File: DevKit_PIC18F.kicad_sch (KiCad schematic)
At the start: 29 parts, among them J1 PIC_ICSP_ICD, J2 USB_B, J3 5P_UART, J4 RA_PORT, J5 RB_PORT, J6 RD_PORT, J7 RC_PORT, J8 RE_PORT, SW1 SW_DIP, X1 16MHz

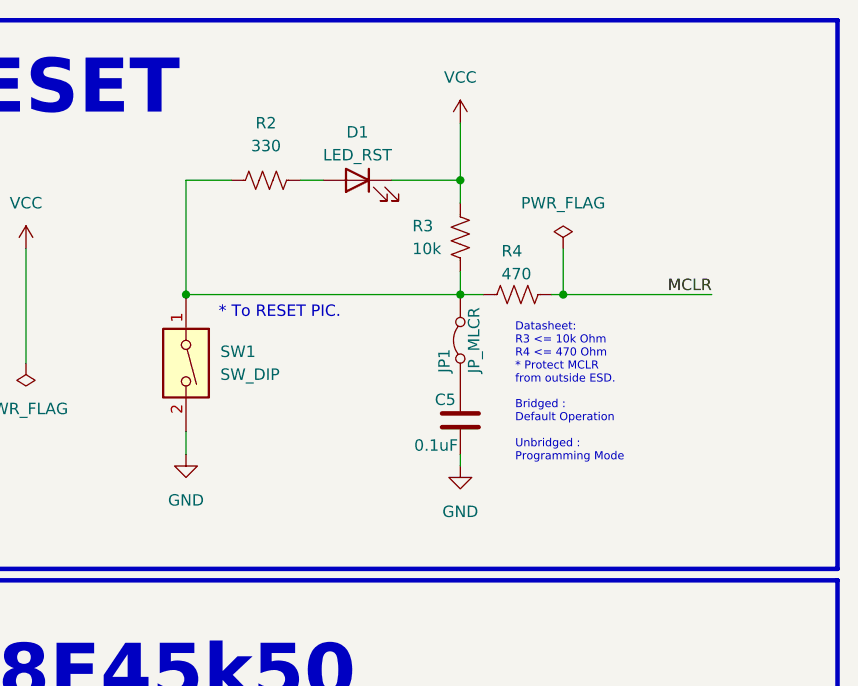
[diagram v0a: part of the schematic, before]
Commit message: Fix Bug : remove bridge as we don't need it.
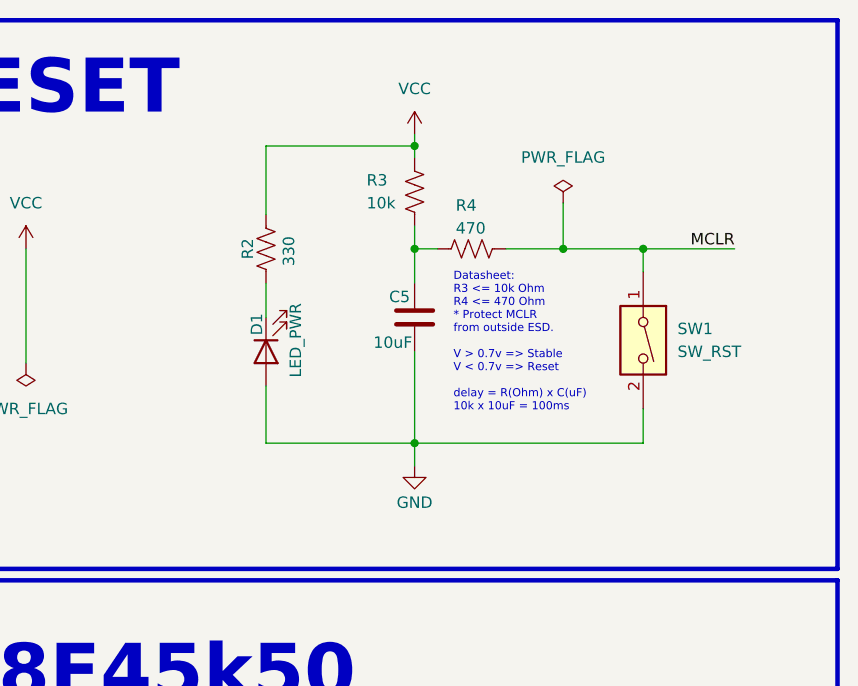
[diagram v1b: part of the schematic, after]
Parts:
- removed JP1: JP_MLCR, Button_Switch_THT:SW_DIP_SPSTx01_Slide_9.78x4.72mm_W7.62mm_P2.54mm, symbol Jumper:Jumper_2_Bridged
- C5: value 0.1uF -> 10uF
- D1: value LED_RST -> LED_PWR
- SW1: value SW_DIP -> SW_RST
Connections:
- net GND: now also D1.2 (A)
- net MCLR: now also SW1.1
- net VCC: now also R2.2; no longer D1.1 (K)
- net at R3.2, R4.2: now also C5.2; no longer R2.1, SW1.1
- new net: D1.1 (K), R2.1
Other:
- note added: "Datasheet: R3 <= 10k Ohm R4 <= 470 Ohm * Protect MCLR from outside ESD. V > 0.7v => Stable V < 0.7v => Reset delay = R(Ohm) x C(uF) 10k x 10uF = 100ms"
- note removed: "* To RESET PIC."
- note removed: "Bridged : Default Operation Unbridged : Programming Mode"
- note removed: "Datasheet: R3 <= 10k Ohm R4 <= 470 Ohm * Protect MCLR from outside ESD."
- moved on the sheet: C5, R3, R4, SW1

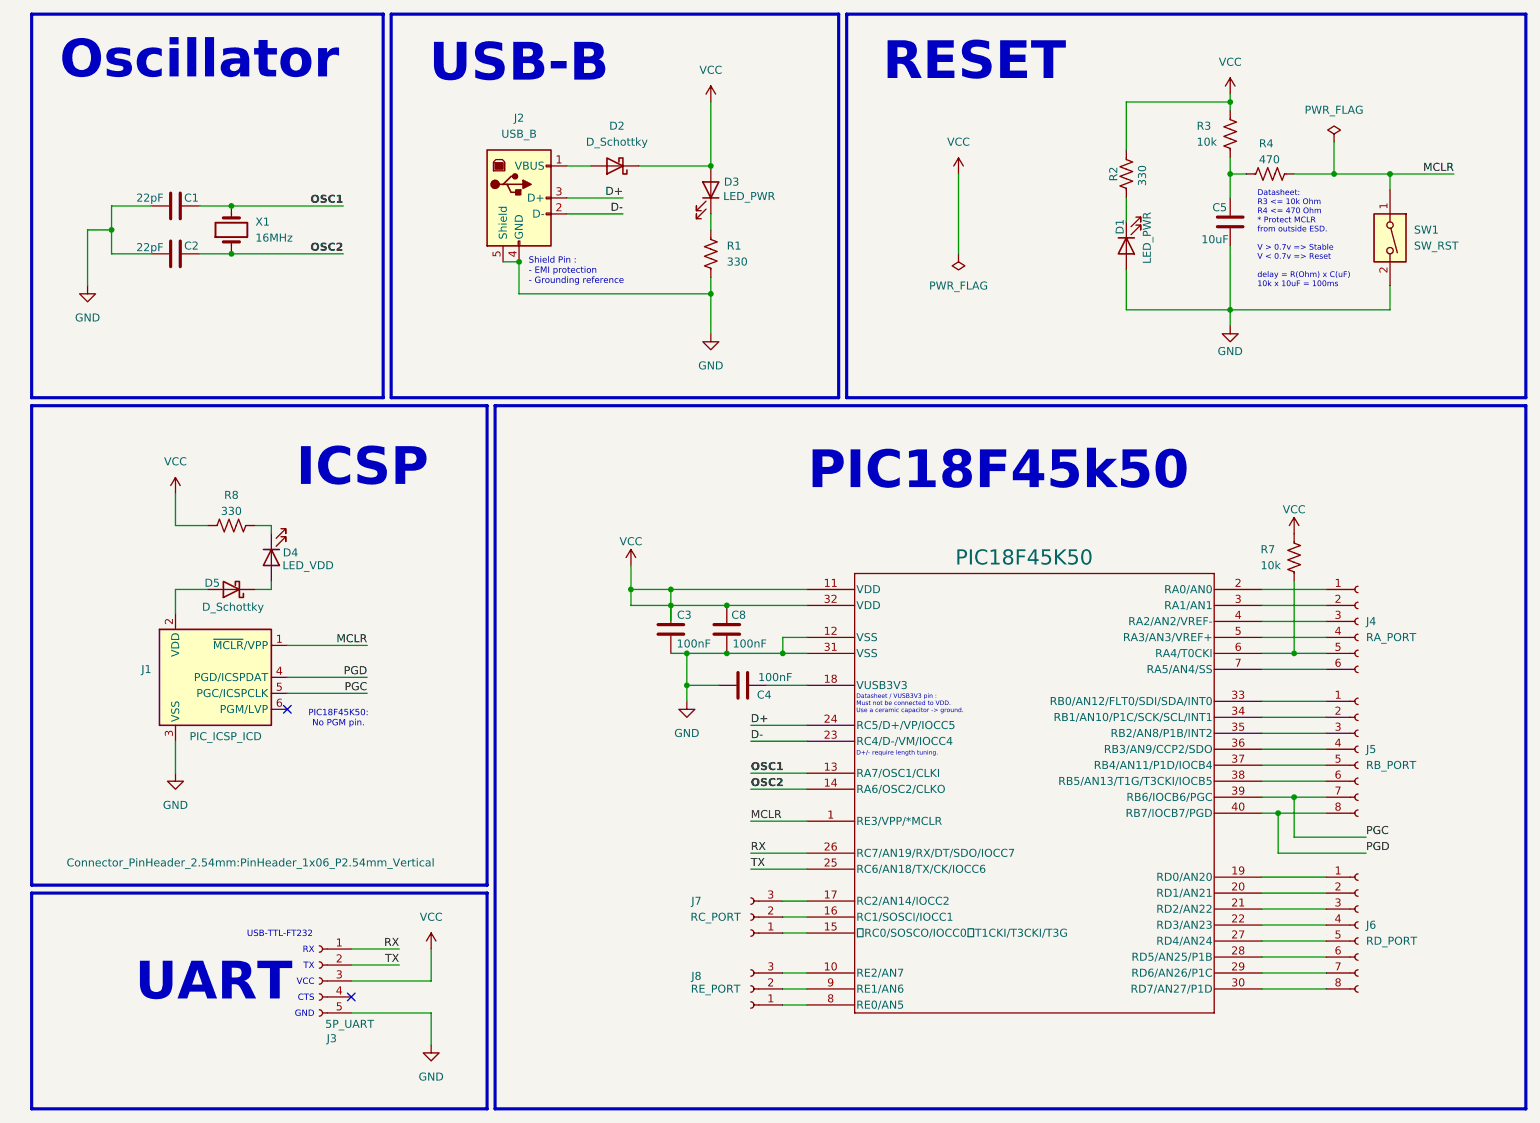
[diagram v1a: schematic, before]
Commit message: Updaet Rev.4 : Flip:ICSP+ Move->LED, +Test_LED->RD0, Group all Resistors.
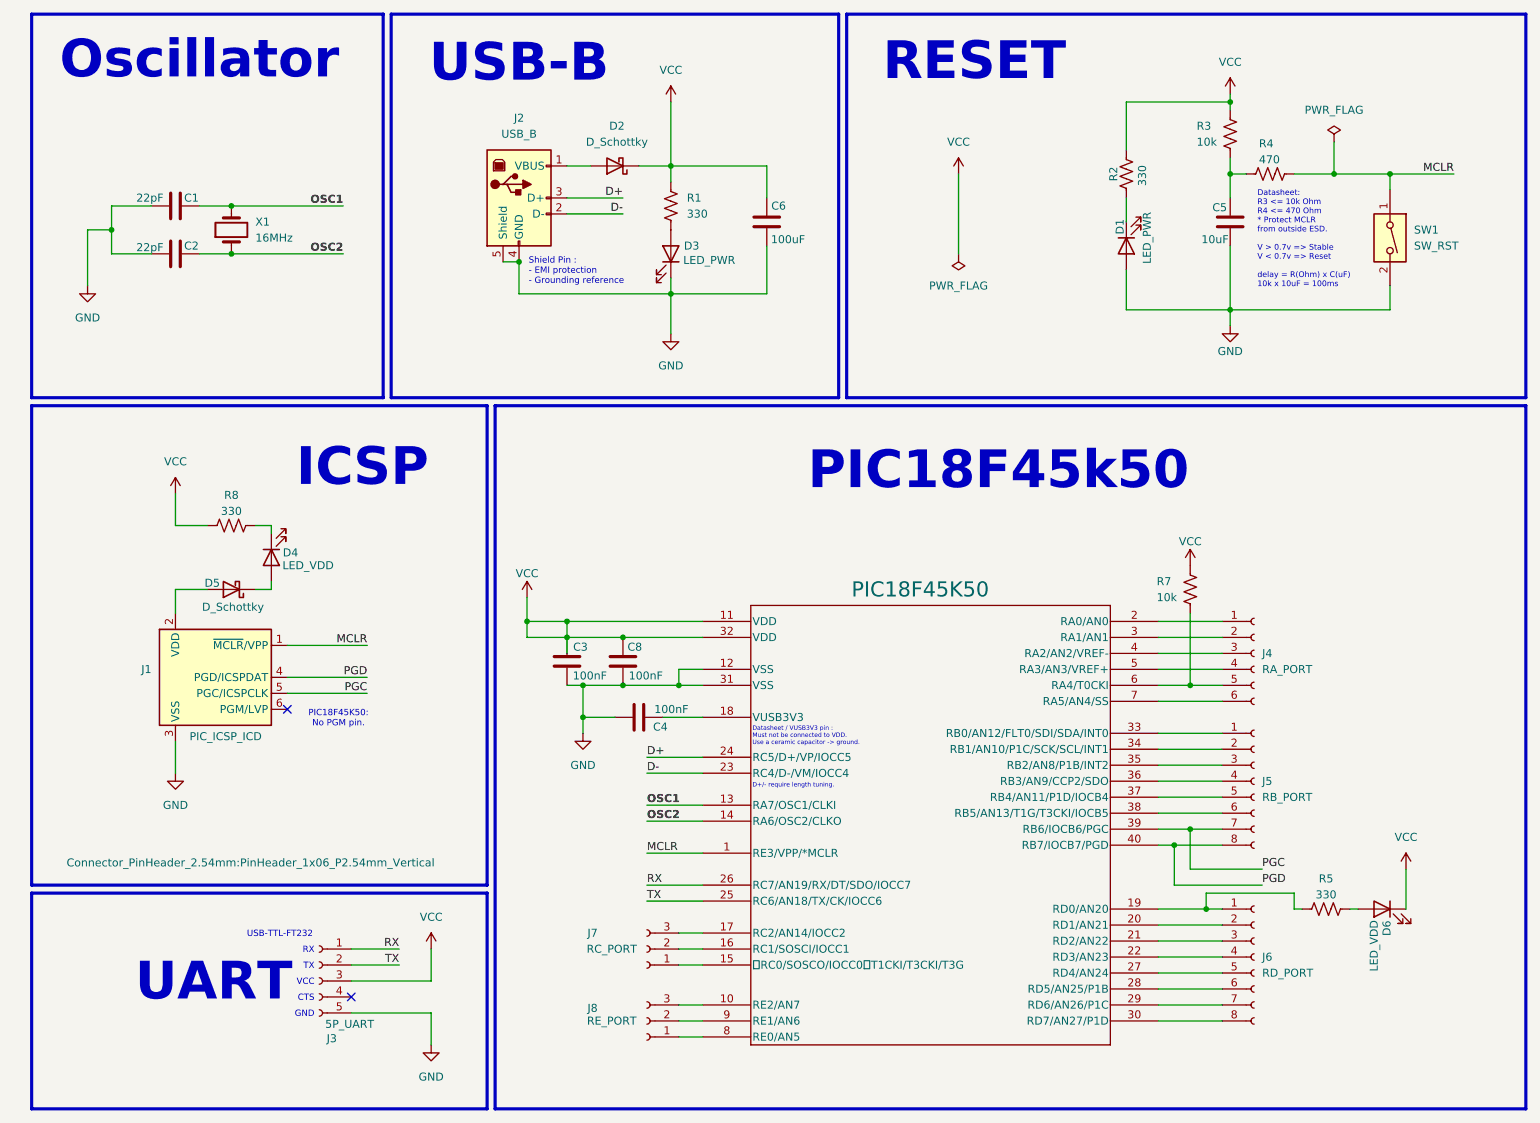
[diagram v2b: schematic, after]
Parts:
- added C6: 100uF, Capacitor_THT:C_Disc_D3.0mm_W1.6mm_P2.50mm, symbol Device:C
- added D6: LED_VDD, LED_THT:LED_D3.0mm_FlatTop, symbol Device:LED
- added R5: 330, Resistor_THT:R_Axial_DIN0204_L3.6mm_D1.6mm_P5.08mm_Horizontal, symbol Device:R_US
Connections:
- net GND: now also D3.1 (K), C6.1; no longer R1.2
- net VCC: now also R1.1, C6.2, D6.1 (K); no longer D3.2 (A)
- net at J6.1 (Pin_1), PIC18F45K50.19 (RD0/AN20): now also R5.1
- new net: D3.2 (A), R1.2
- new net: D6.2 (A), R5.2
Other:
- moved on the sheet: C3, C4, C8, D3, J4, J5, J6, J7, J8, PIC18F45K50, R7

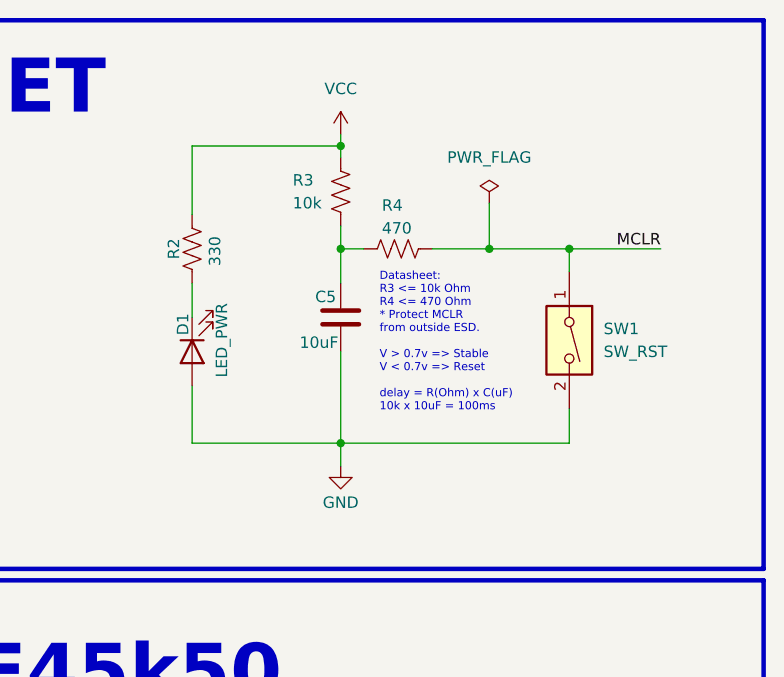
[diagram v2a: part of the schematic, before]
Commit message: Rev.5 : remove redundant LED D1
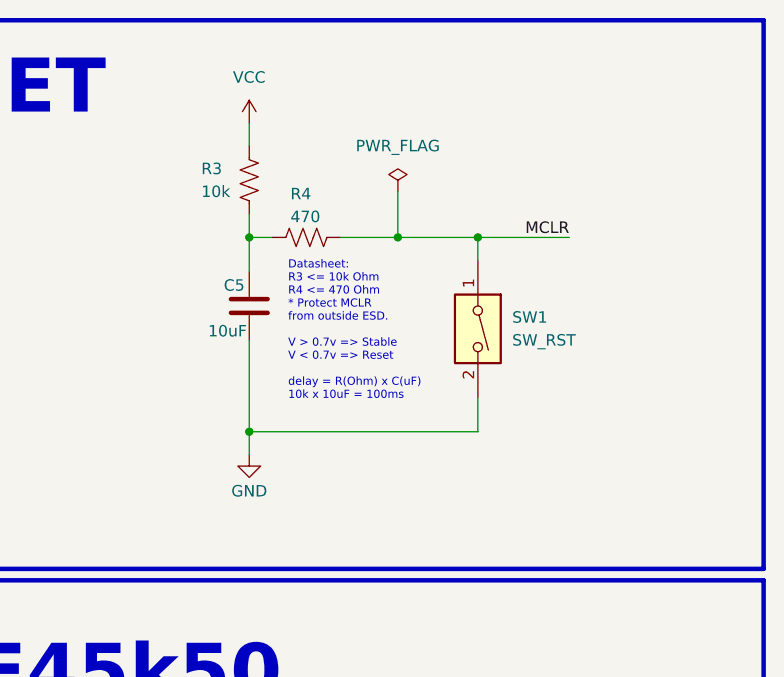
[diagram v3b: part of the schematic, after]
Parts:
- removed D1: LED_PWR, LED_THT:LED_D3.0mm_FlatTop, symbol Device:LED
- removed R2: 330, Resistor_THT:R_Axial_DIN0204_L3.6mm_D1.6mm_P5.08mm_Horizontal, symbol Device:R_US
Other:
- moved on the sheet: C5, R3, R4, SW1

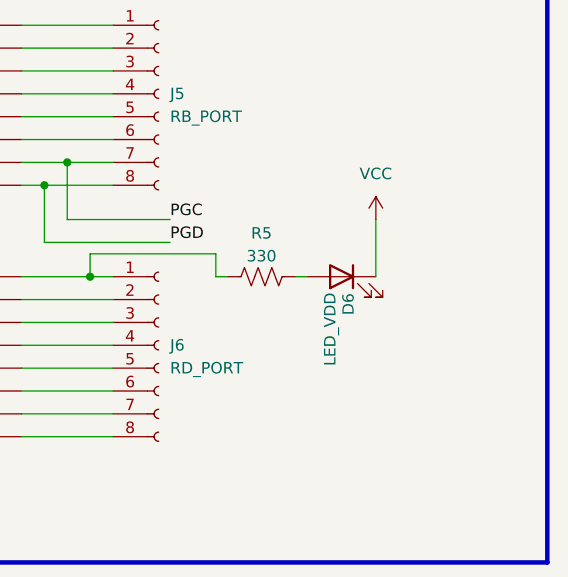
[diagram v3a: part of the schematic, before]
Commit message: rev.6: fixed LED-D6 -> GND instead VCC pull-up style.
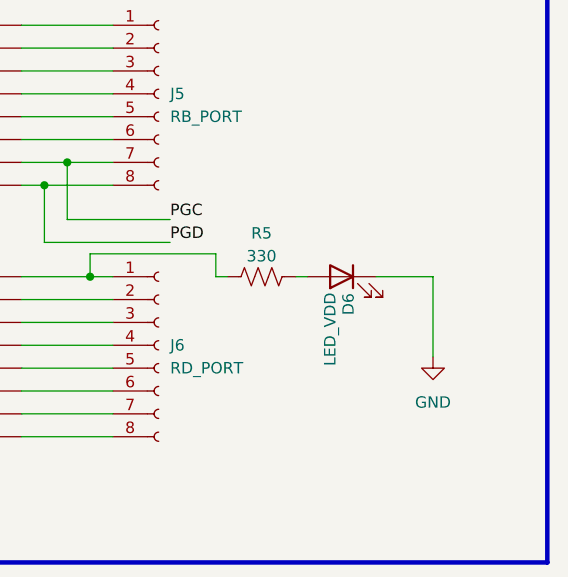
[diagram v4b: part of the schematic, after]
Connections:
- net GND: now also D6.1 (K)
- net VCC: no longer D6.1 (K)
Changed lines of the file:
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@@
+	(wire
+		(pts
+			(xy 238.76 154.94) (xy 238.76 163.83)
+		)
+		(stroke
+			(width 0)
+			(type default)
+		)
+	)
 	(wire
 		(pts
@@
 	(wire
 		(pts
+			(xy 232.41 154.94) (xy 238.76 154.94)
+		)
+		(stroke
+			(width 0)
+			(type default)
+		)
+	)
+	(wire
+		(pts
 			(xy 203.2 116.84) (xy 193.04 116.84)
 		)
@@
 		(pts
 			(xy 203.2 167.64) (xy 193.04 167.64)
-		)
-		(stroke
-			(width 0)
-			(type default)
-		)
-	)
-	(wire
-		(pts
-			(xy 232.41 148.59) (xy 232.41 154.94)
 		)
 		(stroke
@@
 	)
 	(symbol
-		(lib_id "power:VCC")
-		(at 232.41 148.59 0)
-		(mirror y)
-		(unit 1)
-		(exclude_from_sim no)
-		(in_bom yes)
-		(on_board yes)
-		(dnp no)
-		(property "Reference" "#PWR10"
-			(at 232.41 152.4 0)
-			(effects
-				(font
-					(size 1.27 1.27)
-				)
-				(hide yes)
-			)
-		)
-		(property "Value" "VCC"
-			(at 232.41 143.51 0)
-			(effects
-				(font
-					(size 1.27 1.27)
-				)
-			)
-		)
-		(property "Footprint" ""
-			(at 232.41 148.59 0)
-			(effects
-				(font
-					(size 1.27 1.27)
-				)
-				(hide yes)
-			)
-		)
-		(property "Datasheet" ""
-			(at 232.41 148.59 0)
-			(effects
-				(font
-					(size 1.27 1.27)
-				)
-				(hide yes)
-			)
-		)
-		(property "Description" "Power symbol creates a global label with name \"VCC\""
-			(at 232.41 148.59 0)
-			(effects
-				(font
-					(size 1.27 1.27)
-				)
-				(hide yes)
-			)
-		)
-		(pin "1"
-		)
-		(instances
-			(project "DevKit_PIC18F"
-				(path "/495af0d8-3788-4f6a-8ee9-f4c61668daf8"
-					(reference "#PWR10")
-					(unit 1)
-				)
-			)
-		)
-	)
-	(symbol
 		(lib_id "Connector:Conn_01x08_Socket")
 		(at 208.28 162.56 0)
@@
 					(unit 1)
 				)
+			)
+		)
+	)
+	(symbol
+		(lib_id "power:GND")
+		(at 238.76 163.83 0)
+		(unit 1)
+		(exclude_from_sim no)
+		(in_bom yes)
+		(on_board yes)
+		(dnp no)
+		(fields_autoplaced yes)
+		(property "Reference" "#PWR10"
+			(at 238.76 170.18 0)
+			(effects
+				(font
+					(size 1.27 1.27)
+				)
+				(hide yes)
+			)
+		)
+		(property "Value" "GND"
+			(at 238.76 168.91 0)
+			(effects
+				(font
+					(size 1.27 1.27)
+				)
+			)
+		)
+		(property "Footprint" ""
+			(at 238.76 163.83 0)
+			(effects
+				(font
+					(size 1.27 1.27)
+				)
+				(hide yes)
+			)
+		)
+		(property "Datasheet" ""
+			(at 238.76 163.83 0)
+			(effects
+				(font
+					(size 1.27 1.27)
+				)
+				(hide yes)
+			)
+		)
+		(property "Description" "Power symbol creates a global label with name \"GND\" , ground"
+			(at 238.76 163.83 0)
+			(effects
+				(font
+					(size 1.27 1.27)
+				)
+				(hide yes)
+			)
+		)
+		(pin "1"
+		)
+		(instances
+			(project "DevKit_PIC18F"
+				(path "/495af0d8-3788-4f6a-8ee9-f4c61668daf8"
+					(reference "#PWR10")
+					(unit 1)
+				)
